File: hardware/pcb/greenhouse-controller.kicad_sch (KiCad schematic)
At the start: 21 parts, among them J1 Motors A, J2 Screw_Terminal_01x02, J3 I2C Display, J4 Keypad, J5 MODBUS RS485, Q1 2N7000, Q2 2N7000, U1 Wemos_S3_ESP32-S3, U2 BUCK-30V-5V

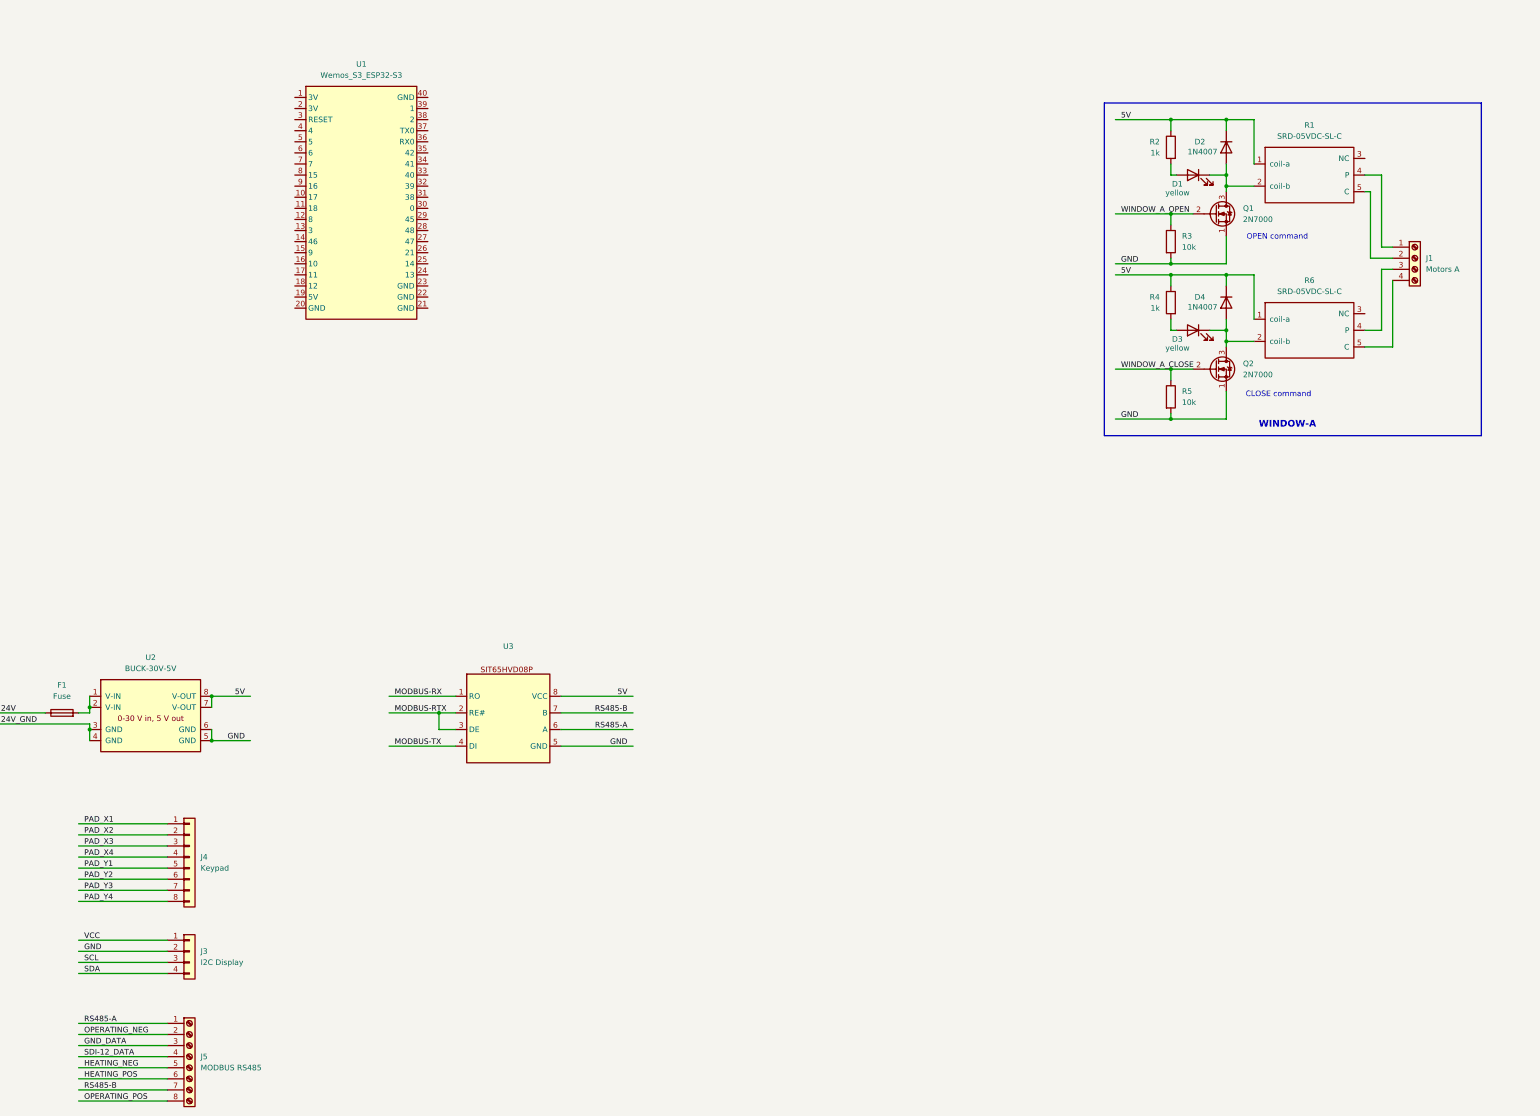
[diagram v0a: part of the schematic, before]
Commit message: Working code on DS1307 RTC
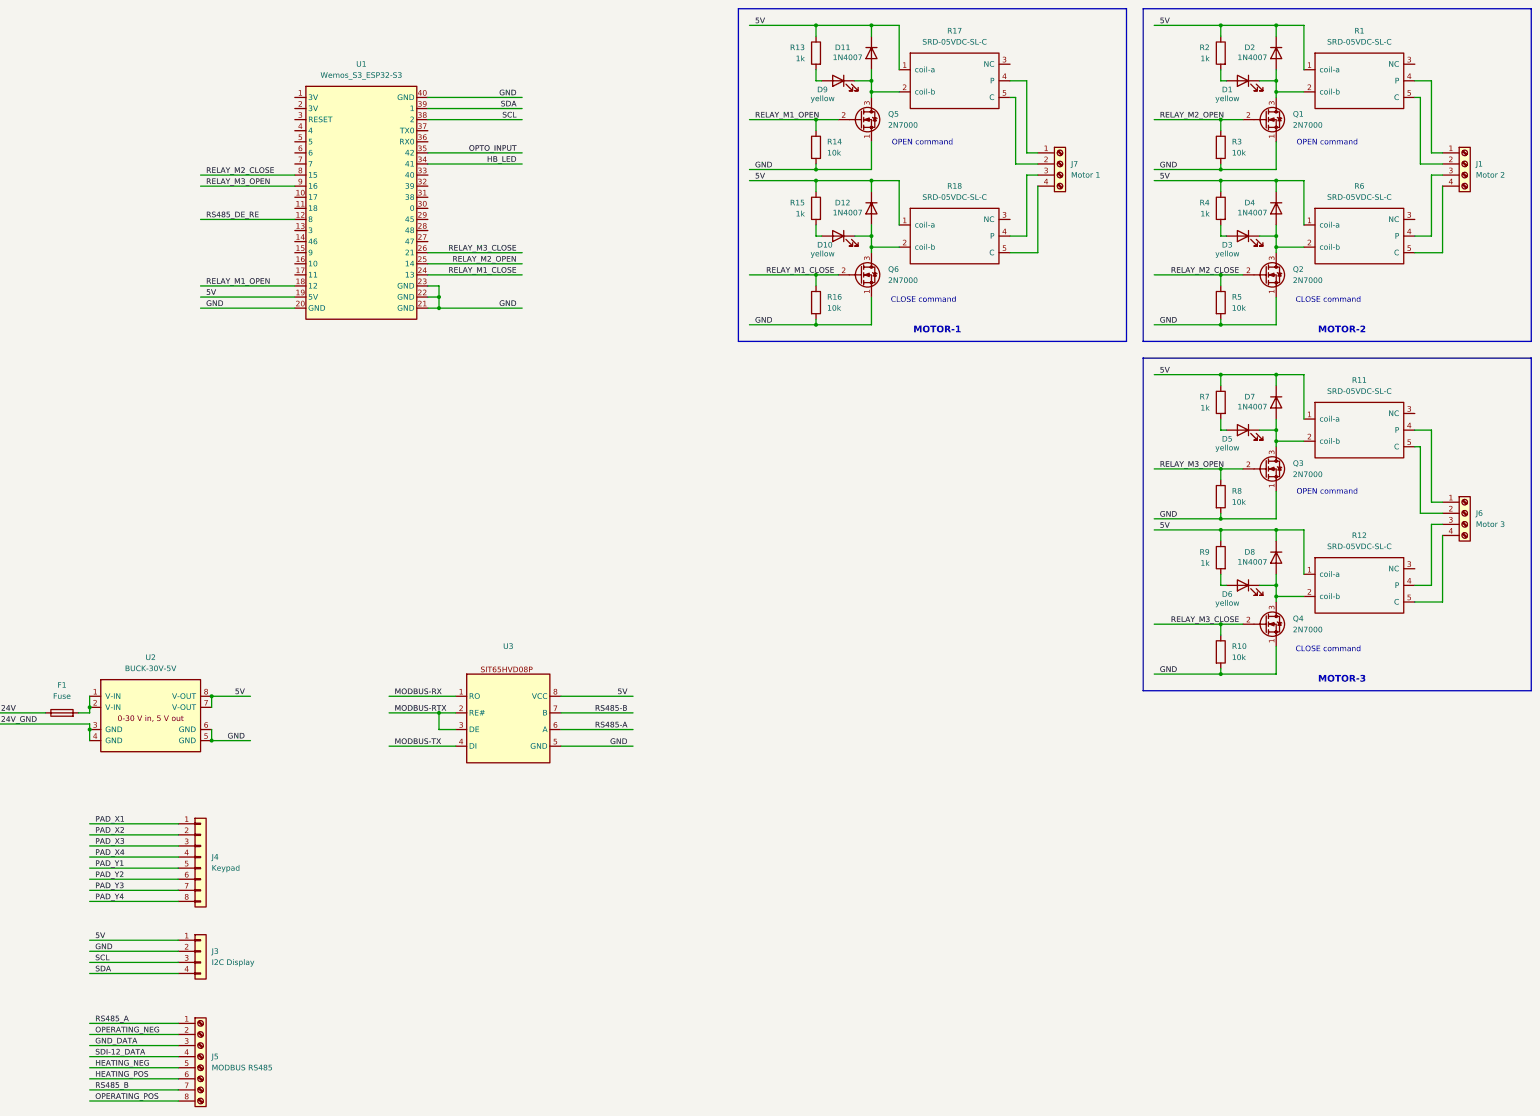
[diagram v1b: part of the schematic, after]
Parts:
- added D10, D5, D6, D9: yellow, symbol Device:LED
- added D11, D12, D7, D8: 1N4007, Diode_THT:D_DO-41_SOD81_P10.16mm_Horizontal, symbol Diode:1N4007
- added J6: Motor 3, symbol Connector:Screw_Terminal_01x04
- added J7: Motor 1, symbol Connector:Screw_Terminal_01x04
- added Q3, Q4, Q5, Q6: 2N7000, Package_TO_SOT_THT:TO-92_Inline, symbol Transistor_FET:2N7000
- added R10, R14, R16, R8: 10k, symbol Device:R
- added R11, R12, R17, R18: SRD-05VDC-SL-C, symbol my-KiCad-library:SRD-05VDC-SL-C
- added R13, R15, R7, R9: 1k, symbol Device:R
- J1: value Motors A -> Motor 2
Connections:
- net VCC is gone; now on net 5V: J3.1 (Pin_1)
- net WINDOW_A_CLOSE is gone; now on net RELAY_M2_CLOSE: Q2.2 (G), R5.1
- net WINDOW_A_OPEN is gone; now on net RELAY_M2_OPEN: Q1.2 (G), R3.1
- net 5V: now also U1.19 (5V), D11.1 (K), D12.1 (K), D7.1 (K), D8.1 (K), R11.1 (coil-a), R12.1 (coil-a), R13.1, R15.1, R17.1 (coil-a), R18.1 (coil-a), R7.1, R9.1
- net GND: now also U1.20 (GND), U1.21 (GND), U1.22 (GND), U1.23 (GND), U1.40 (GND), Q3.1 (S), Q4.1 (S), Q5.1 (S), Q6.1 (S), R10.2, R14.2, R16.2, R8.2
- net RS485-A: no longer J5.1 (Pin_1)
- net RS485-B: no longer J5.7 (Pin_7)
- net SCL: now also U1.38 (2)
- net SDA: now also U1.39 (1)
- net RS485_DE_RE: now reaches U1.12 (8)
- net at U1.18 (12): no longer names the net of U1.18 (12)
- net at U1.18 (12): now also Q5.2 (G), R14.1
- net RELAY_M1_CLOSE: now reaches U1.24 (13)
- net RELAY_M1_CLOSE: now also Q6.2 (G), R16.1
- net RELAY_M2_OPEN: now reaches U1.25 (14)
- net RELAY_M3_CLOSE: now reaches U1.26 (21)
- net RELAY_M3_CLOSE: now also Q4.2 (G), R10.1
- net HB_LED: now reaches U1.34 (41)
- net OPTO_INPUT: now reaches U1.35 (42)
- net RELAY_M2_CLOSE: now reaches U1.8 (15)
- net RELAY_M3_OPEN: now reaches U1.9 (16)
- net RELAY_M3_OPEN: now also Q3.2 (G), R8.1
- new net: D5.1 (K), D7.2 (A), Q3.3 (D), R11.2 (coil-b)
- new net: D9.2 (A), R13.2
- new net: D10.1 (K), D12.2 (A), Q6.3 (D), R18.2 (coil-b)
- new net: J7.3 (Pin_3), R18.4 (P)
- new net: J7.4 (Pin_4), R18.5 (C)
- new net: J7.1 (Pin_1), R17.4 (P)
- new net: J7.2 (Pin_2), R17.5 (C)
- new net: D6.1 (K), D8.2 (A), Q4.3 (D), R12.2 (coil-b)
- new net: J6.3 (Pin_3), R12.4 (P)
- new net: J6.4 (Pin_4), R12.5 (C)
- new net: D10.2 (A), R15.2
- new net: J6.1 (Pin_1), R11.4 (P)
- new net: J6.2 (Pin_2), R11.5 (C)
- new net: D6.2 (A), R9.2
- new net: D11.2 (A), D9.1 (K), Q5.3 (D), R17.2 (coil-b)
- new net: D5.2 (A), R7.2
- new net RS485_A: J5.1 (Pin_1)
- new net RS485_B: J5.7 (Pin_7)
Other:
- note added: "MOTOR-1"
- note added: "MOTOR-2"
- note added: "MOTOR-3"
- note removed: "WINDOW-A"
- moved on the sheet: D1, D2, D3, D4, J1, J3, J4, J5, Q1, Q2, R1, R2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

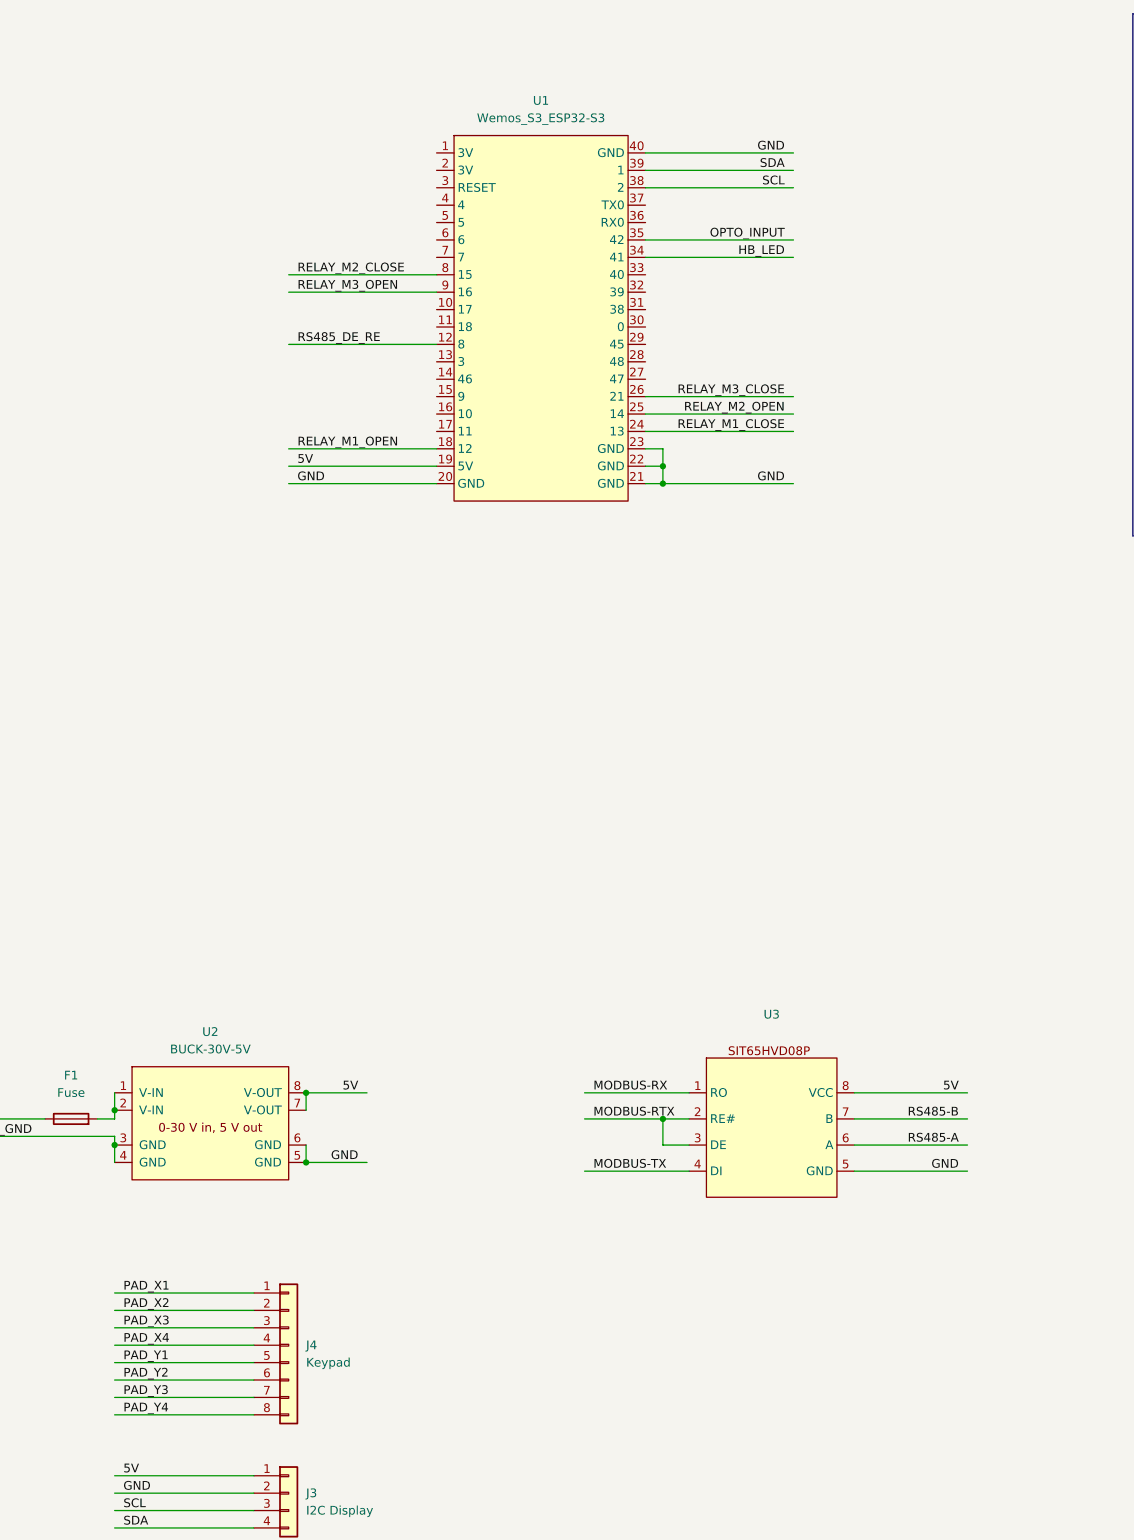
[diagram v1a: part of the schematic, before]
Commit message: Added working driver for keypad and name change to rtc type used
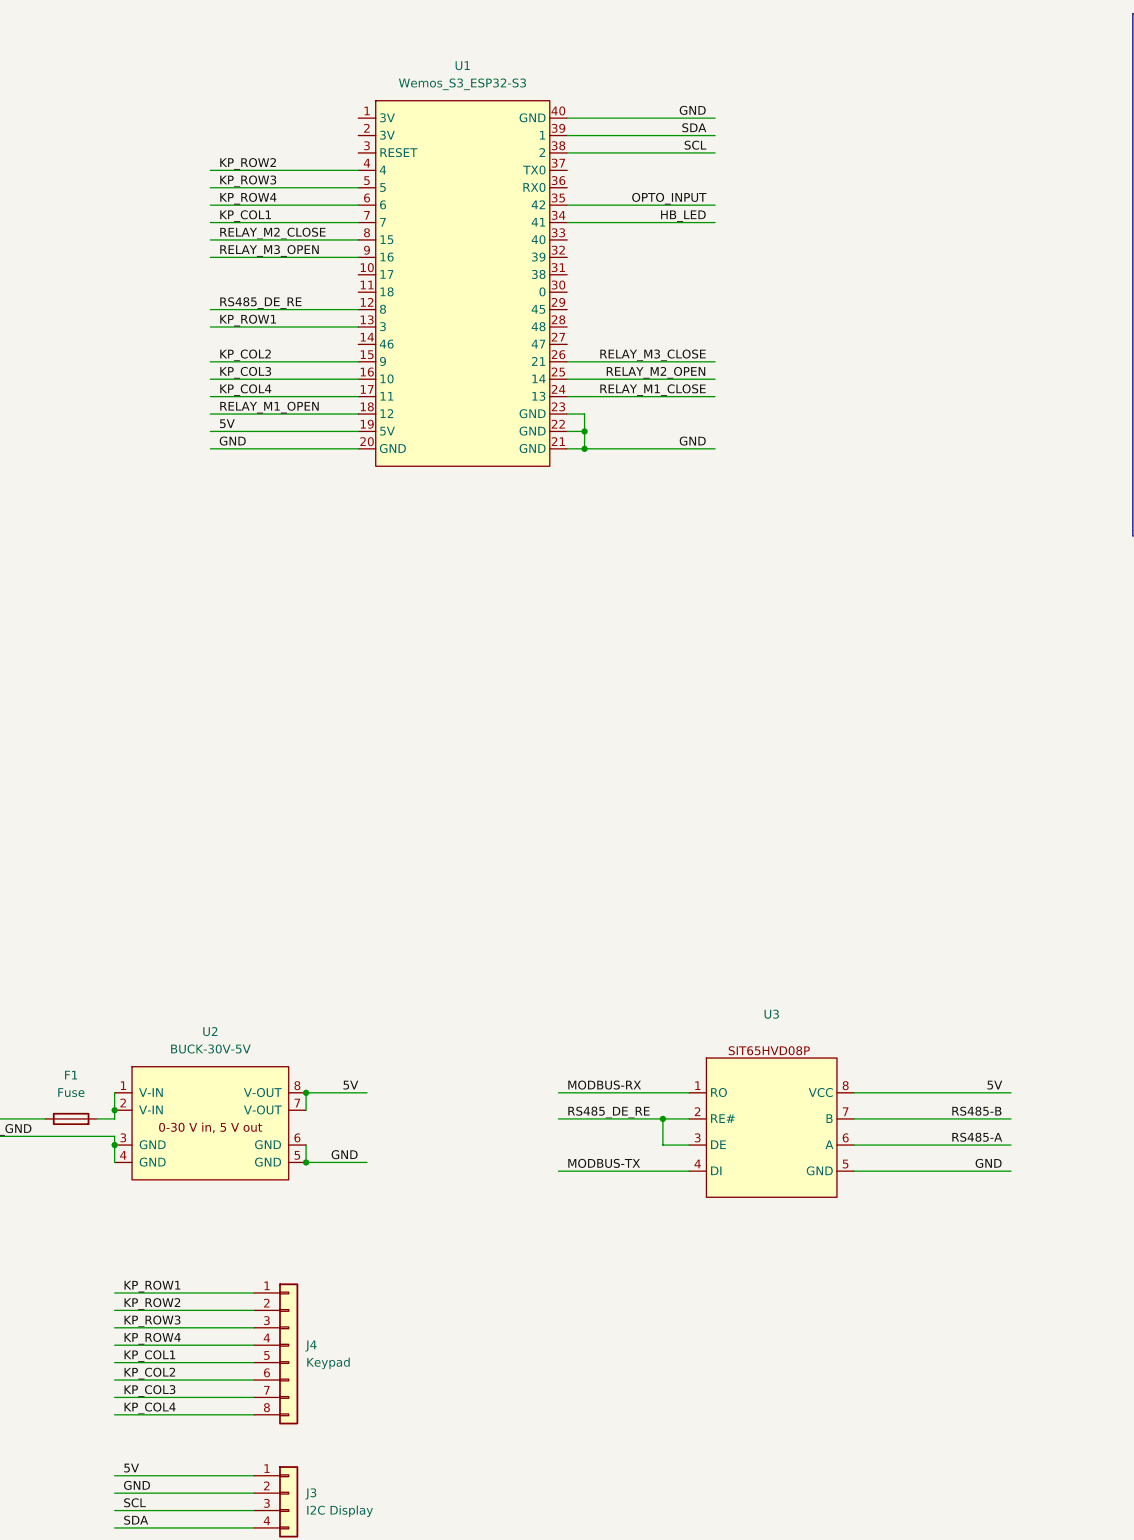
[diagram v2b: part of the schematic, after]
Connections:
- net MODBUS-RTX is gone; now on net RS485_DE_RE: U3.2 (RE#), U3.3 (DE)
- net PAD_X1 is gone; now on net KP_ROW1: J4.1 (Pin_1)
- net PAD_X2 is gone; now on net KP_ROW2: J4.2 (Pin_2)
- net PAD_X3 is gone; now on net KP_ROW3: J4.3 (Pin_3)
- net PAD_X4 is gone; now on net KP_ROW4: J4.4 (Pin_4)
- net PAD_Y1 is gone; now on net KP_COL1: J4.5 (Pin_5)
- net PAD_Y2 is gone; now on net KP_COL2: J4.6 (Pin_6)
- net PAD_Y3 is gone; now on net KP_COL3: J4.7 (Pin_7)
- net PAD_Y4 is gone; now on net KP_COL4: J4.8 (Pin_8)
- net KP_ROW1: now reaches U1.13 (3)
- net KP_COL2: now reaches U1.15 (9)
- net KP_COL3: now reaches U1.16 (10)
- net KP_COL4: now reaches U1.17 (11)
- net KP_ROW2: now reaches U1.4
- net KP_ROW3: now reaches U1.5
- net KP_ROW4: now reaches U1.6
- net KP_COL1: now reaches U1.7
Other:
- moved on the sheet: U1
